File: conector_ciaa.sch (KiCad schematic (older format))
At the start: 1 part

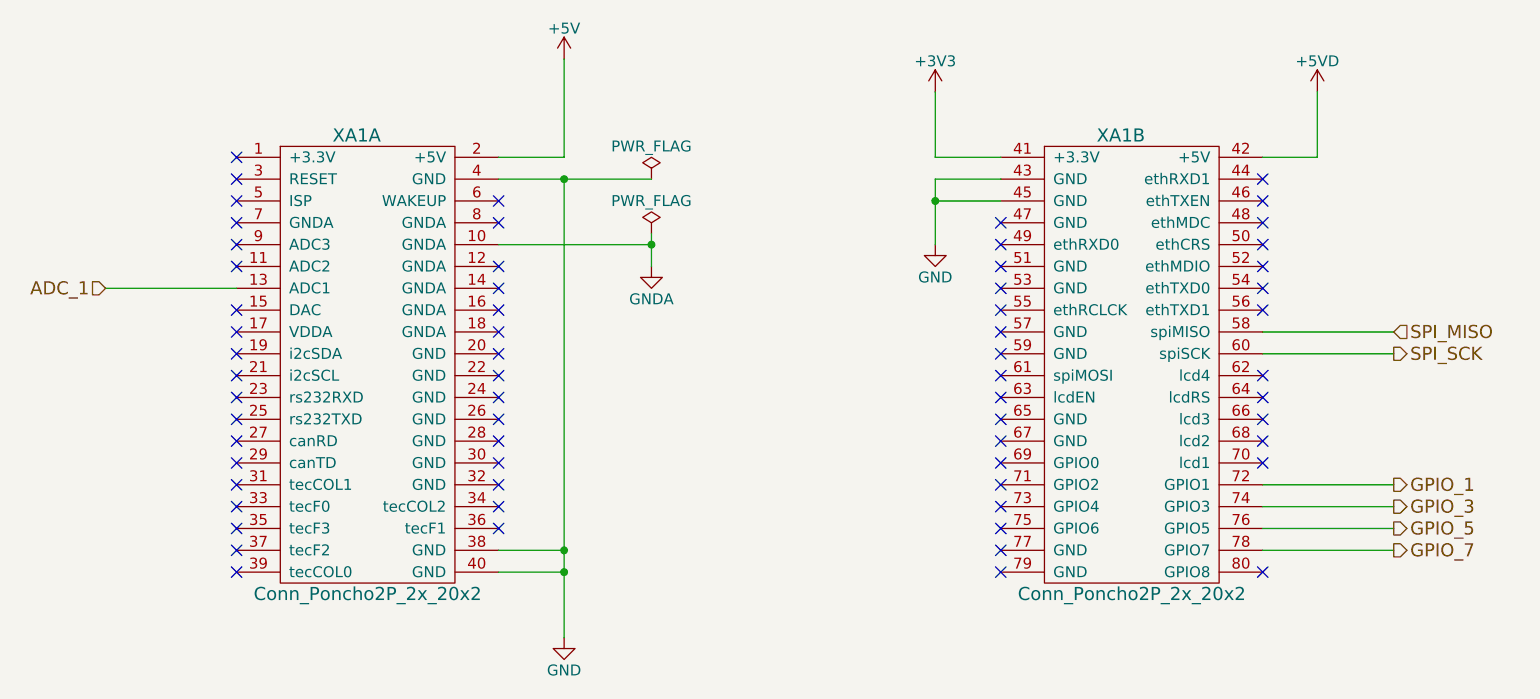
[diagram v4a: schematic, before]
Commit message: Correccion Final
Se trabajo sobre correcciones de 2da revision. Se agregaron archivos gerbers, BOM, y objetos 3D
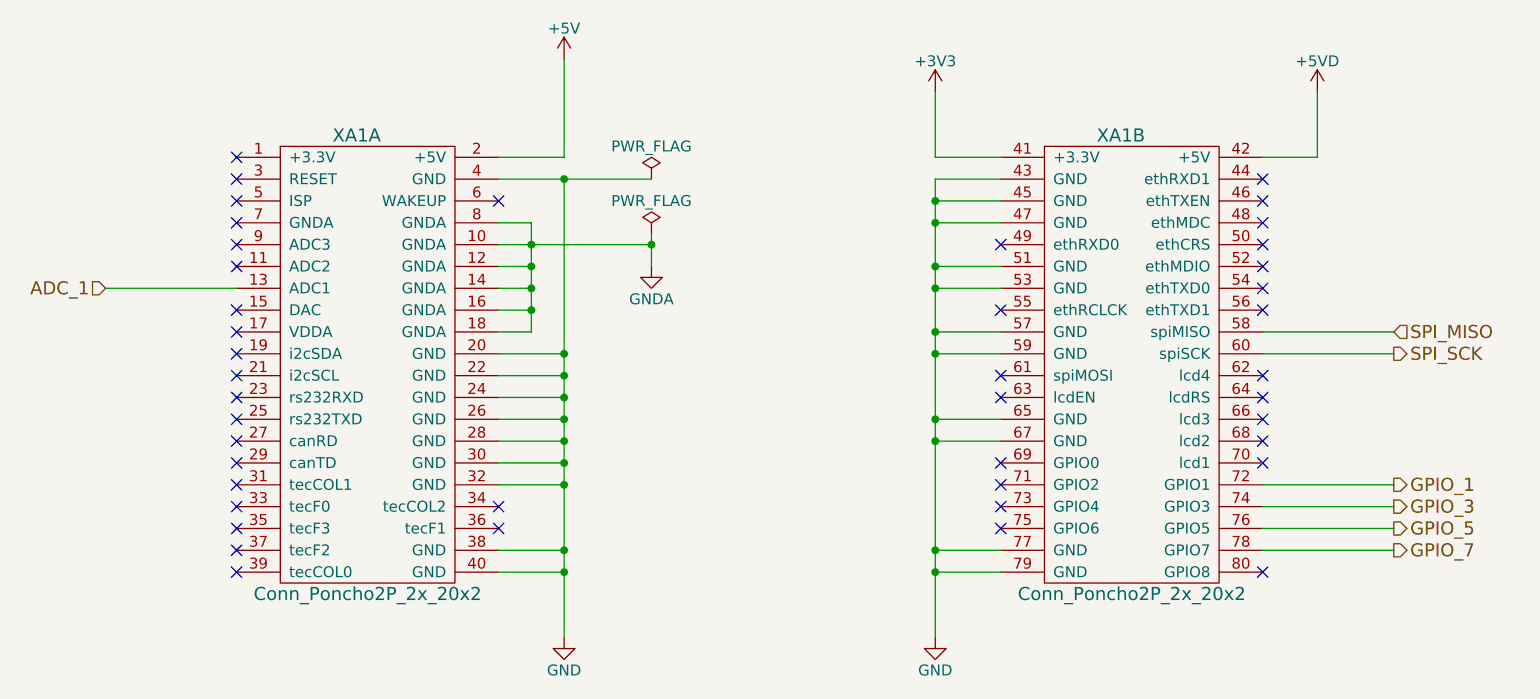
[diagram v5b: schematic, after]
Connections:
- net GND: now also XA1.20 (GND), XA1.22 (GND), XA1.24 (GND), XA1.26 (GND), XA1.28 (GND), XA1.30 (GND), XA1.32 (GND), XA1.47 (GND), XA1.51 (GND), XA1.53 (GND), XA1.57 (GND), XA1.59 (GND), XA1.65 (GND), XA1.67 (GND), XA1.77 (GND), XA1.79 (GND)
- net GNDA: now also XA1.12 (GNDA), XA1.14 (GNDA), XA1.16 (GNDA), XA1.18 (GNDA), XA1.8 (GNDA)
- no-connect marks 64 -> 43
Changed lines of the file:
@@
 EESchema Schematic File Version 2
 LIBS:TempRelay
-LIBS:power
-LIBS:tempRelayPoncho-cache
 EELAYER 25 0
 EELAYER END
@@
 $Comp
 L Conn_Poncho2P_2x_20x2 XA1
-U 1 1 594C48CD
-P 3650 2500
-F 0 "XA1" H 3950 2900 60  0000 C CNN
-F 1 "Conn_Poncho2P_2x_20x2" H 4000 800 60  0000 C CNN
-F 2 "footprints:Conn_Poncho_Completo" H 3650 2500 60  0001 C CNN
-F 3 "" H 3650 2500 60  0000 C CNN
-F 4 "Value" H 3650 2500 60  0001 C CNN "Manf"
-F 5 "Value" H 3650 2500 60  0001 C CNN "Manf#"
-F 6 "Value" H 3650 2500 60  0001 C CNN "Digikey#"
-F 7 "Value" H 3650 2500 60  0001 C CNN "Mouser#"
-F 8 "Value" H 3650 2500 60  0001 C CNN "Description"
-	1    3650 2500
-	1    0    0    -1
-$EndComp
-$Comp
-L Conn_Poncho2P_2x_20x2 XA1
 U 2 1 594C49E3
 P 7150 2500
@@
 	1    0    0    -1
 $EndComp
-Wire Wire Line
-	3400 2800 2800 2800
-Wire Wire Line
-	8100 3000 8700 3000
-Wire Wire Line
-	8100 3100 8700 3100
 Text HLabel 8700 3700 2    60   Output ~ 0
 GPIO_1
@@
 Text HLabel 2800 2800 0    60   Input ~ 0
 ADC_1
-Wire Wire Line
-	4600 2300 5300 2300
-Wire Wire Line
-	4900 2300 4900 4400
-Wire Wire Line
-	4900 4000 4600 4000
-Wire Wire Line
-	4900 4100 4600 4100
-Connection ~ 4900 4000
-Connection ~ 4900 4100
 NoConn ~ 4600 2400
-NoConn ~ 4600 2700
-NoConn ~ 4600 2800
-NoConn ~ 4600 2900
-NoConn ~ 4600 3000
 NoConn ~ 4600 3800
 NoConn ~ 4600 3900
@@
 NoConn ~ 3400 4000
 NoConn ~ 3400 4100
-Wire Wire Line
-	6900 2300 6600 2300
-Connection ~ 6600 2400
 NoConn ~ 6900 2600
 NoConn ~ 6900 2900
@@
 $EndComp
 $Comp
-L GND #PWR09
+L GND #PWR08
 U 1 1 594EB35A
-P 6600 2600
-F 0 "#PWR09" H 6600 2350 50  0001 C CNN
-F 1 "GND" H 6600 2450 50  0000 C CNN
-F 2 "" H 6600 2600 50  0001 C CNN
-F 3 "" H 6600 2600 50  0001 C CNN
-	1    6600 2600
-	1    0    0    -1
-$EndComp
-$Comp
-L +5V #PWR010
+P 6600 4400
+F 0 "#PWR08" H 6600 4150 50  0001 C CNN
+F 1 "GND" H 6600 4250 50  0000 C CNN
+F 2 "" H 6600 4400 50  0001 C CNN
+F 3 "" H 6600 4400 50  0001 C CNN
+	1    6600 4400
+	1    0    0    -1
+$EndComp
+$Comp
+L +5V #PWR09
 U 1 1 594EB38C
 P 4900 1750
-F 0 "#PWR010" H 4900 1600 50  0001 C CNN
+F 0 "#PWR09" H 4900 1600 50  0001 C CNN
 F 1 "+5V" H 4900 1890 50  0000 C CNN
 F 2 "" H 4900 1750 50  0001 C CNN
@@
 	1    0    0    -1
 $EndComp
-NoConn ~ 4600 2500
-$Comp
-L PWR_FLAG #FLG011
+$Comp
+L PWR_FLAG #FLG010
 U 1 1 594EBA4F
 P 5300 2300
-F 0 "#FLG011" H 5300 2375 50  0001 C CNN
+F 0 "#FLG010" H 5300 2375 50  0001 C CNN
 F 1 "PWR_FLAG" H 5300 2450 50  0000 C CNN
 F 2 "" H 5300 2300 50  0001 C CNN
@@
 	1    0    0    -1
 $EndComp
-Connection ~ 4900 2300
 NoConn ~ 3400 2500
-Wire Wire Line
-	4600 2600 5300 2600
-$Comp
-L GNDA #PWR012
+$Comp
+L GNDA #PWR011
 U 1 1 5962BA55
 P 5300 2700
-F 0 "#PWR012" H 5300 2450 50  0001 C CNN
+F 0 "#PWR011" H 5300 2450 50  0001 C CNN
 F 1 "GNDA" H 5300 2550 50  0000 C CNN
 F 2 "" H 5300 2700 50  0001 C CNN
@@
 	1    0    0    -1
 $EndComp
-Wire Wire Line
-	5300 2550 5300 2700
-$Comp
-L PWR_FLAG #FLG013
+$Comp
+L PWR_FLAG #FLG012
 U 1 1 59630D10
 P 5300 2550
-F 0 "#FLG013" H 5300 2625 50  0001 C CNN
+F 0 "#FLG012" H 5300 2625 50  0001 C CNN
 F 1 "PWR_FLAG" H 5300 2700 50  0000 C CNN
 F 2 "" H 5300 2550 50  0001 C CNN
@@
 	1    0    0    -1
 $EndComp
-Connection ~ 5300 2600
 NoConn ~ 6900 3600
 NoConn ~ 6900 3700
-Wire Wire Line
-	8700 3700 8100 3700
-Wire Wire Line
-	8100 3800 8700 3800
-Wire Wire Line
-	8700 3900 8100 3900
-Wire Wire Line
-	8100 4000 8700 4000
-Wire Wire Line
-	4900 1750 4900 2200
-Wire Wire Line
-	4900 2200 4600 2200
-Wire Wire Line
-	8350 1900 8350 2200
-Wire Wire Line
-	8350 2200 8100 2200
-$Comp
-L +5VD #PWR014
+$Comp
+L +5VD #PWR013
 U 1 1 596C77DA
 P 8350 1900
-F 0 "#PWR014" H 8350 1750 50  0001 C CNN
+F 0 "#PWR013" H 8350 1750 50  0001 C CNN
 F 1 "+5VD" H 8350 2040 50  0000 C CNN
 F 2 "" H 8350 1900 50  0001 C CNN
@@
 	1    0    0    -1
 $EndComp
-Wire Wire Line
-	6900 2200 6600 2200
-Wire Wire Line
-	6600 2200 6600 1900
-$Comp
-L +3V3 #PWR015
+$Comp
+L +3V3 #PWR014
 U 1 1 596C783A
 P 6600 1900
-F 0 "#PWR015" H 6600 1750 50  0001 C CNN
+F 0 "#PWR014" H 6600 1750 50  0001 C CNN
 F 1 "+3V3" H 6600 2040 50  0000 C CNN
 F 2 "" H 6600 1900 50  0001 C CNN
@@
 $EndComp
 NoConn ~ 3400 2200
-NoConn ~ 4600 3100
-NoConn ~ 4600 3200
-NoConn ~ 4600 3300
-NoConn ~ 4600 3400
-NoConn ~ 4600 3500
-NoConn ~ 4600 3600
-NoConn ~ 4600 3700
-Wire Wire Line
-	6600 2300 6600 2600
-NoConn ~ 6900 2700
-NoConn ~ 6900 2500
-NoConn ~ 6900 2800
-NoConn ~ 6900 3000
-NoConn ~ 6900 3100
-NoConn ~ 6900 3400
-NoConn ~ 6900 3500
-NoConn ~ 6900 4000
-NoConn ~ 6900 4100
+$Comp
+L Conn_Poncho2P_2x_20x2 XA1
+U 1 1 594C48CD
+P 3650 2500
+F 0 "XA1" H 3950 2900 60  0000 C CNN
+F 1 "Conn_Poncho2P_2x_20x2" H 4000 800 60  0000 C CNN
+F 2 "footprints:Conn_Poncho_Completo" H 3650 2500 60  0001 C CNN
+F 3 "" H 3650 2500 60  0000 C CNN
+F 4 "Value" H 3650 2500 60  0001 C CNN "Manf"
+F 5 "Value" H 3650 2500 60  0001 C CNN "Manf#"
+F 6 "Value" H 3650 2500 60  0001 C CNN "Digikey#"
+F 7 "Value" H 3650 2500 60  0001 C CNN "Mouser#"
+F 8 "Value" H 3650 2500 60  0001 C CNN "Description"
+	1    3650 2500
+	1    0    0    -1
+$EndComp
+Wire Wire Line
+	3400 2800 2800 2800
+Wire Wire Line
+	8100 3000 8700 3000
+Wire Wire Line
+	8100 3100 8700 3100
+Wire Wire Line
+	4600 2300 5300 2300
+Wire Wire Line
+	4900 4000 4600 4000
+Wire Wire Line
+	4900 4100 4600 4100
+Wire Wire Line
+	6900 2300 6600 2300
+Connection ~ 6600 2400
+Wire Wire Line
+	4600 2600 5300 2600
+Wire Wire Line
+	5300 2550 5300 2700
+Connection ~ 5300 2600
+Wire Wire Line
+	8700 3700 8100 3700
+Wire Wire Line
+	8100 3800 8700 3800
+Wire Wire Line
+	8700 3900 8100 3900
+Wire Wire Line
+	8100 4000 8700 4000
+Wire Wire Line
+	8350 1900 8350 2200
+Wire Wire Line
+	8350 2200 8100 2200
+Wire Wire Line
+	6900 2200 6600 2200
+Wire Wire Line
+	6600 2200 6600 1900
+Wire Wire Line
+	6600 2300 6600 4400
 Wire Wire Line
 	6900 2400 6600 2400
+Wire Wire Line
+	4900 2300 4900 4400
+Connection ~ 4900 4100
+Connection ~ 4900 2300
+Connection ~ 4900 4000
+Wire Wire Line
+	4600 2200 4900 2200
+Wire Wire Line
+	4900 2200 4900 1750
+Wire Wire Line
+	4600 2500 4750 2500
+Wire Wire Line
+	4750 2500 4750 3000
+Connection ~ 4750 2600
+Wire Wire Line
+	4750 2700 4600 2700
+Wire Wire Line
+	4750 2800 4600 2800
+Connection ~ 4750 2700
+Wire Wire Line
+	4750 2900 4600 2900
+Connection ~ 4750 2800
+Wire Wire Line
+	4750 3000 4600 3000
+Connection ~ 4750 2900
+Wire Wire Line
+	4600 3100 4900 3100
+Connection ~ 4900 3100
+Wire Wire Line
+	4600 3200 4900 3200
+Connection ~ 4900 3200
+Wire Wire Line
+	4600 3300 4900 3300
+Connection ~ 4900 3300
+Wire Wire Line
+	4600 3400 4900 3400
+Connection ~ 4900 3400
+Wire Wire Line
+	4600 3500 4900 3500
+Connection ~ 4900 3500
+Wire Wire Line
+	4600 3600 4900 3600
+Connection ~ 4900 3600
+Wire Wire Line
+	4600 3700 4900 3700
+Connection ~ 4900 3700
+Wire Wire Line
+	6900 2500 6600 2500
+Connection ~ 6600 2500
+Wire Wire Line
+	6900 4100 6600 4100
+Connection ~ 6600 4100
+Wire Wire Line
+	6900 4000 6600 4000
+Connection ~ 6600 4000
+Wire Wire Line
+	6900 3500 6600 3500
+Connection ~ 6600 3500
+Wire Wire Line
+	6900 3400 6600 3400
+Connection ~ 6600 3400
+Wire Wire Line
+	6900 3100 6600 3100
+Connection ~ 6600 3100
+Wire Wire Line
+	6900 3000 6600 3000
+Connection ~ 6600 3000
+Wire Wire Line
+	6900 2800 6600 2800
+Connection ~ 6600 2800
+Wire Wire Line
+	6900 2700 6600 2700
+Connection ~ 6600 2700
 $EndSCHEMATC
